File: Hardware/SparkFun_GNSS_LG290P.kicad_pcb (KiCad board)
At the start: 4 copper layers, 43.2 x 43.2 mm, 135 parts, among them J1 USB_C_Receptacle, J10 Conn_01x06, J2 Conn_01x06, J3 SMA_Edge, J4 Qwiic_RA, J5 SMA_Edge, J6 Conn_01x09, J7 Qwiic_RA, J8 JST_Locking_4, J9 I2C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

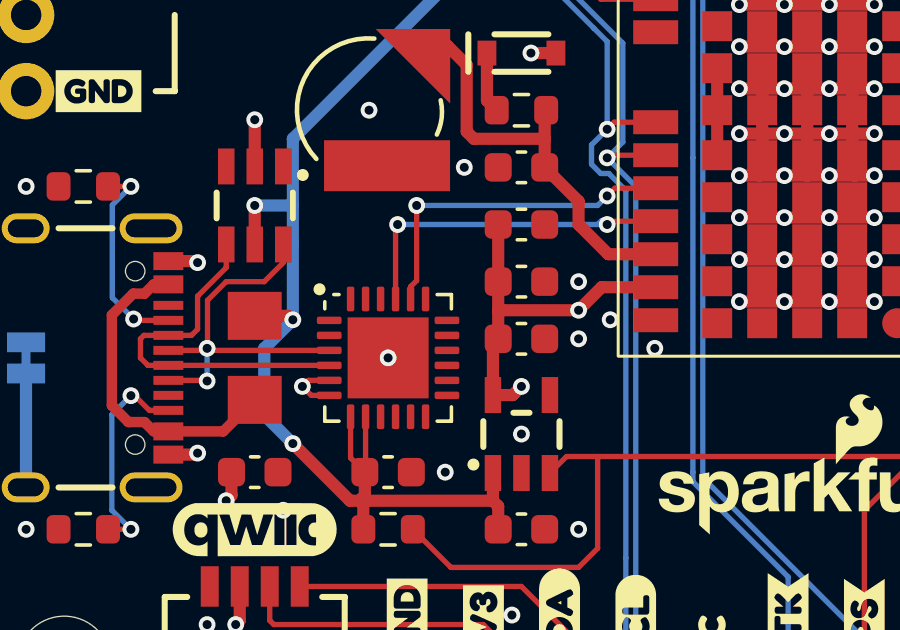
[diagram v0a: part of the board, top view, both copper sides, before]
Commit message: Connect CH342 V3 to decoupling cap
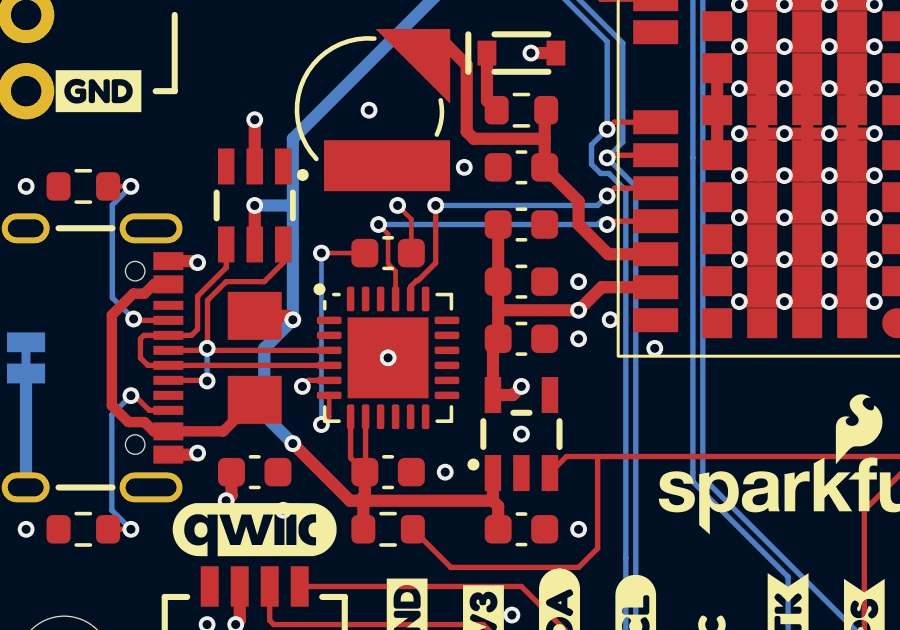
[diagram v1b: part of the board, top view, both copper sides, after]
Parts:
- added C10: 0.1uF, SparkFun-Capacitor:C_0603_1608Metric, F.Cu at (148.6, 101.3)
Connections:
- J8 pad NC1: (no net) -> unconnected-(J8-NC-PadNC1)
- U4 pad 6: 3.3V -> Net-(U4-V3)
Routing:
- net Net-(U4-V3): track 0.00 -> 8.24 mm, vias 0 -> 2
- net GND: track 63.5 -> 65.3 mm, vias 100 -> 101
- net 3.3V: track 24.7 -> 23.7 mm
- net RXD1: track 11.3 -> 12.1 mm

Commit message: Reduce ground clearance to clear DRC error
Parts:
- J3, J5: value SMA_Edge -> Val**

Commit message: Add TVS to 3V3 and VBATT. Add protocol spec.
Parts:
- added D6: PESD0603-240, SparkFun-Capacitor:C_0603_1608Metric, F.Cu at (155.6, 107.3)
- added D7: PESD0603-240, SparkFun-Capacitor:C_0603_1608Metric, F.Cu at (153.0, 92.7)
- turned C8 to 180 degrees
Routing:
- net GND: track 65.3 -> 79.0 mm, vias 101 -> 103
- net V_BCKP: track 13.7 -> 16.0 mm
- net 3V3_EN: track 33.6 -> 32.1 mm
- net 3.3V: track 23.7 -> 24.5 mm, vias 10 -> 11

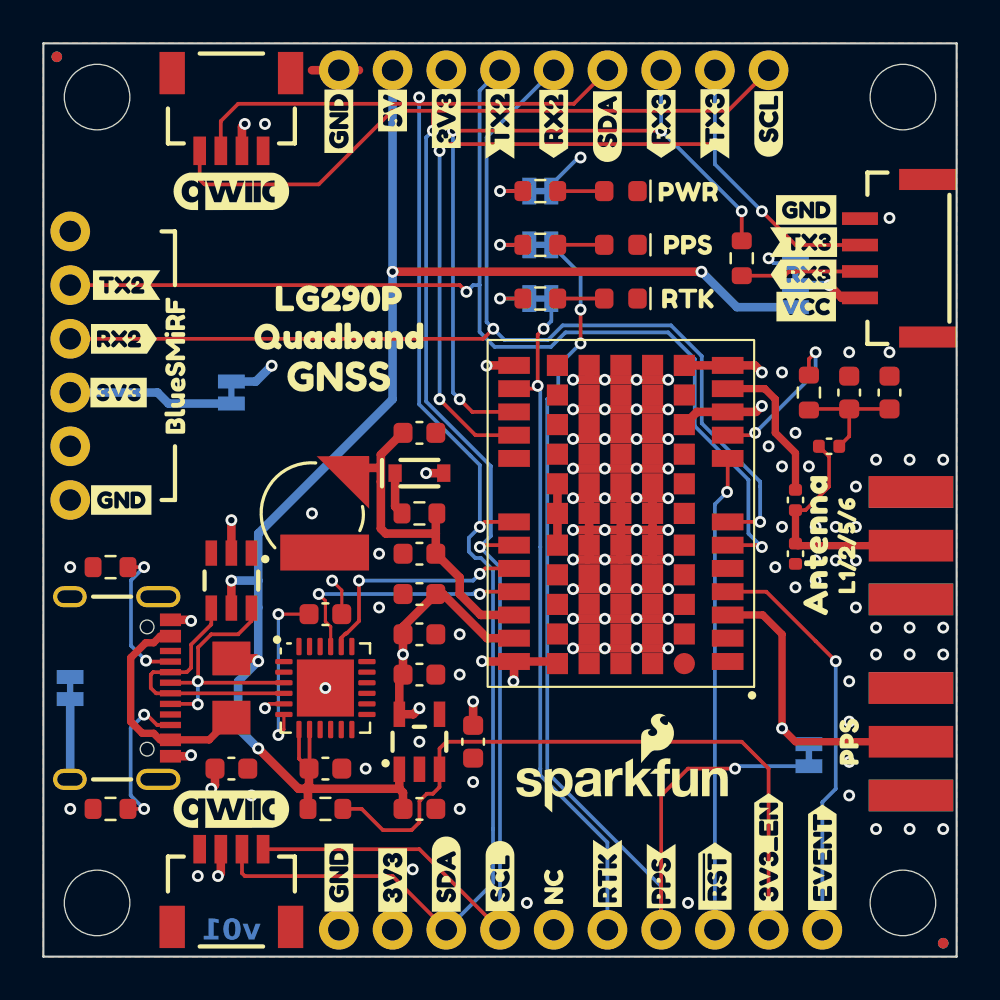
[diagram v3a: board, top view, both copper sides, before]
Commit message: Make post design review changes. Add panel files.
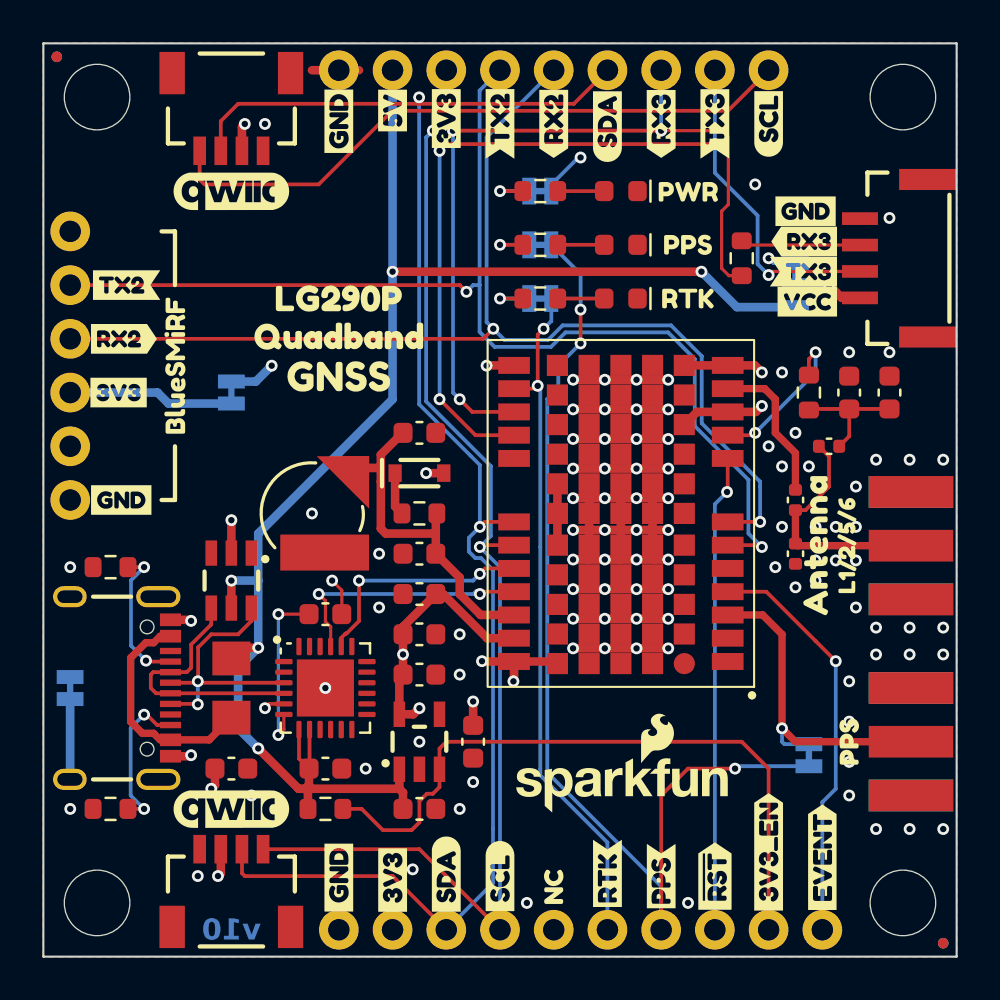
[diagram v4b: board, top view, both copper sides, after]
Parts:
- C13: value 0.1uF -> 1.0uF
- J3, J5: value Val** -> SMA_Edge
- R4: value 1k -> 4.7k
- R9: value 10k -> 100k
- U2: value AP2112K-3.3 -> RT9080-3.3
- moved kibuzzard-66CB3C73 1.56 mm to (171.2, 83.7)
- moved kibuzzard-66CB3C6B 1.40 mm to (171.2, 85.1)
- moved kibuzzard-66CB830B 0.32 mm to (170.8, 88.6)
- moved kibuzzard-66CB37CC 0.23 mm to (171.4, 86.5)
- moved kibuzzard-66CB37D7 0.07 mm to (171.3, 82.2)
- turned R8 to 90 degrees
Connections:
- J8 pad 2: Net-(J8-Pin_2) -> TXD3
- J8 pad 3: TXD3 -> Net-(J8-Pin_3)
- R8 pad 2: Net-(J8-Pin_2) -> Net-(J8-Pin_3)
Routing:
- net Net-(J8-Pin_3): track 0.00 -> 5.67 mm
- net Net-(J8-Pin_2): track 5.67 -> 0.00 mm
- net RXD3: track 35.1 -> 39.3 mm, vias 4 -> 3
- net TXD3: track 42.0 -> 44.2 mm
- net GND: vias 103 -> 104
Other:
- rule pad_to_mask_clearance: 0 -> 0.05
- board text added: "v10"
- board text removed: "v01"

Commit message: Update SparkFun_GNSS_LG290P.kicad_pcb
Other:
- board text added: "Controlled Impedance: JLC04161H-7628"
- board text removed: "Controlled Impedance: JLC7628"
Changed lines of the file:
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@@
 		)
 	)
-	(gr_text "Controlled Impedance: JLC7628"
+	(gr_text "Controlled Impedance: JLC04161H-7628"
 		(at 236.22 172.085 0)
 		(layer "F.Fab")
